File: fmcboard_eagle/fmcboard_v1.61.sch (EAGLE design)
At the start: 208 parts, among them IC1 OPA699ID, IC10 LM358, IC11 7805TV, IC12 SN74AUC2G66DCTR, IC13 SN74AUC2G66DCTR, IC14 SN74AUC2G66DCTR, IC15 SN74AUC2G66DCTR, IC16 DAC7578SPWR, IC17 SN74AUC2G66DCTR, IC18 SN74AUC2G66DCTR, IC19 SN74AUC2G66DCTR, IC2 DAC7578SPWR, IC20 SN74AUC2G66DCTR, IC21 74AUP2GU04GW, IC22 74AUP2GU04GW, IC23 74AUP2GU04GW, IC24 74AUP2GU04GW, IC25 LM358, IC26 AMS1117-1.8, IC3 LTC6229IMS8E#TRPBF, IC4 LTC6229IMS8E#TRPBF, IC5 LTC6229IMS8E#TRPBF, IC6 OPA699ID, IC7 OPA699ID, IC8 LM358, IC9 LM358, J1 8pin, J10 8pin, J11 8pin, J12 4p-2.54, J2 ASP-134604-01, J3 4p-2.54, J4 4p-2.54, J5 8pin, J6 4p-2.54, J7 4p-2.54, J8 4p-2.54, J9 8pin, U1 TXS0108EPWR, U2 STMICROELECTRONICS_L7905ACVST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

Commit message: smd inductors
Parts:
- L1, L2: device rcl:L-US6000-XXX-RC -> SparkFun-Passives:INDUCTOR1210
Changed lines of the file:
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@@
 <part name="SUPPLY30" library="supply2" library_urn="urn:adsk.eagle:library:372" deviceset="GND" device=""/>
 <part name="SUPPLY31" library="supply2" library_urn="urn:adsk.eagle:library:372" deviceset="GND" device=""/>
-<part name="L1" library="rcl" library_urn="urn:adsk.eagle:library:334" deviceset="L-US" device="6000-XXX-RC" package3d_urn="urn:adsk.eagle:package:23538/1" value="10uH"/>
-<part name="L2" library="rcl" library_urn="urn:adsk.eagle:library:334" deviceset="L-US" device="6000-XXX-RC" package3d_urn="urn:adsk.eagle:package:23538/1" value="10uH"/>
+<part name="L1" library="SparkFun-Passives" deviceset="INDUCTOR" device="1210" value="10uH"/>
+<part name="L2" library="SparkFun-Passives" deviceset="INDUCTOR" device="1210" value="10uH"/>
 <part name="C42" library="SparkFun-Passives" deviceset="CAP" device="0805" value="0.1uF"/>
 <part name="C43" library="SparkFun-Passives" deviceset="CAP" device="0805" value="0.1uF"/>

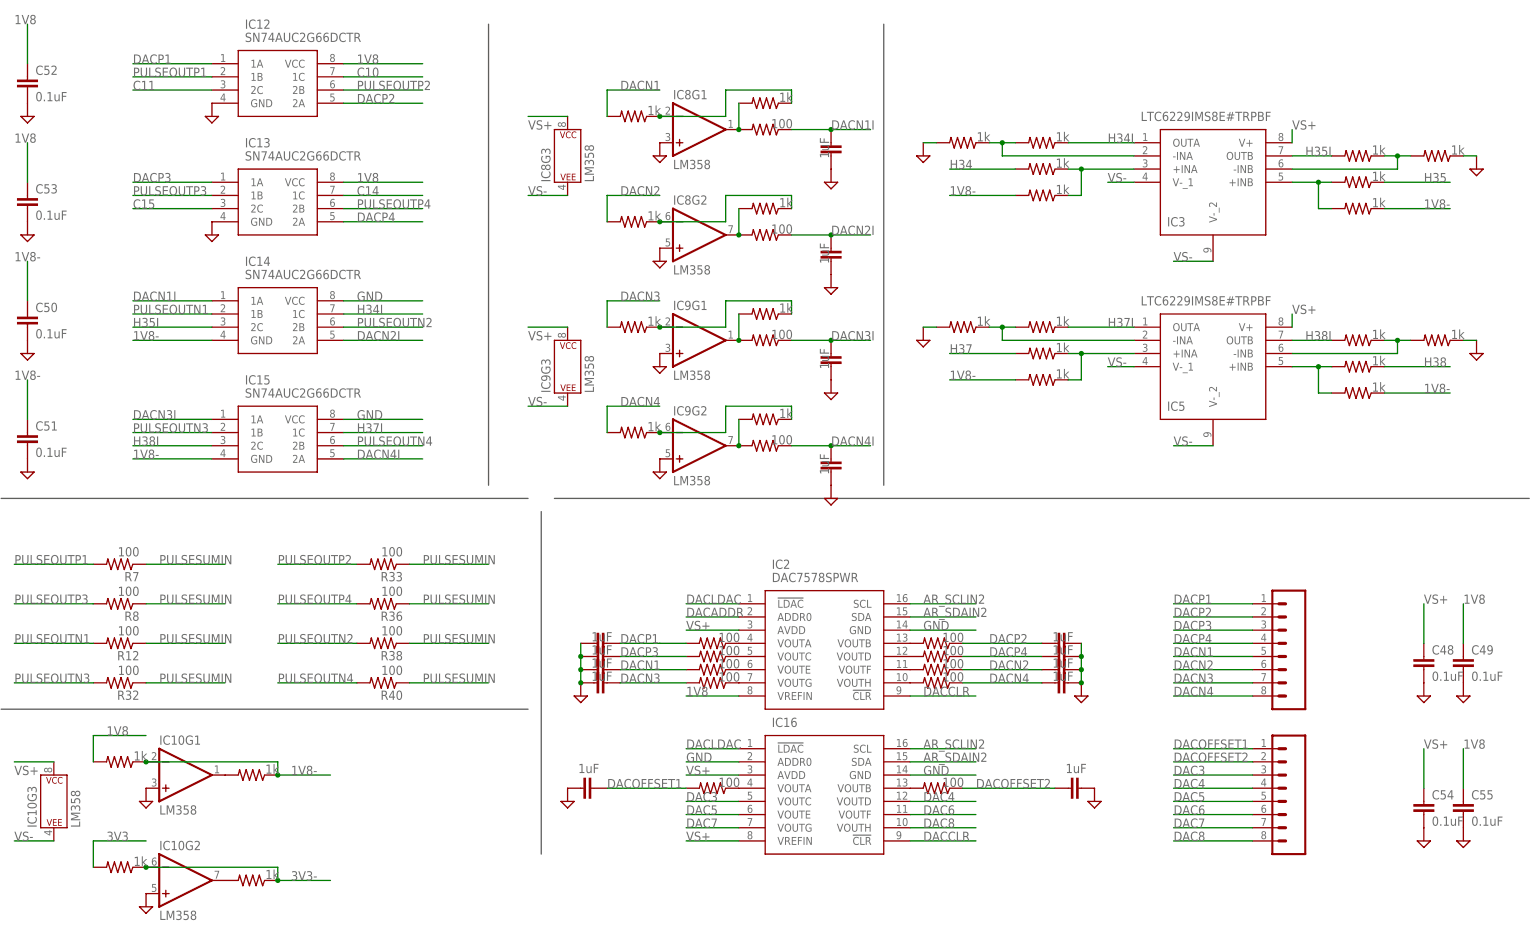
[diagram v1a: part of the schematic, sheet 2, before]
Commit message: v1.61: Fix 1v8- 1k->330 fo 16 100->330 for 9 1pF and 10k pulldown on opin 10k pulldowns on neg pulse inputs
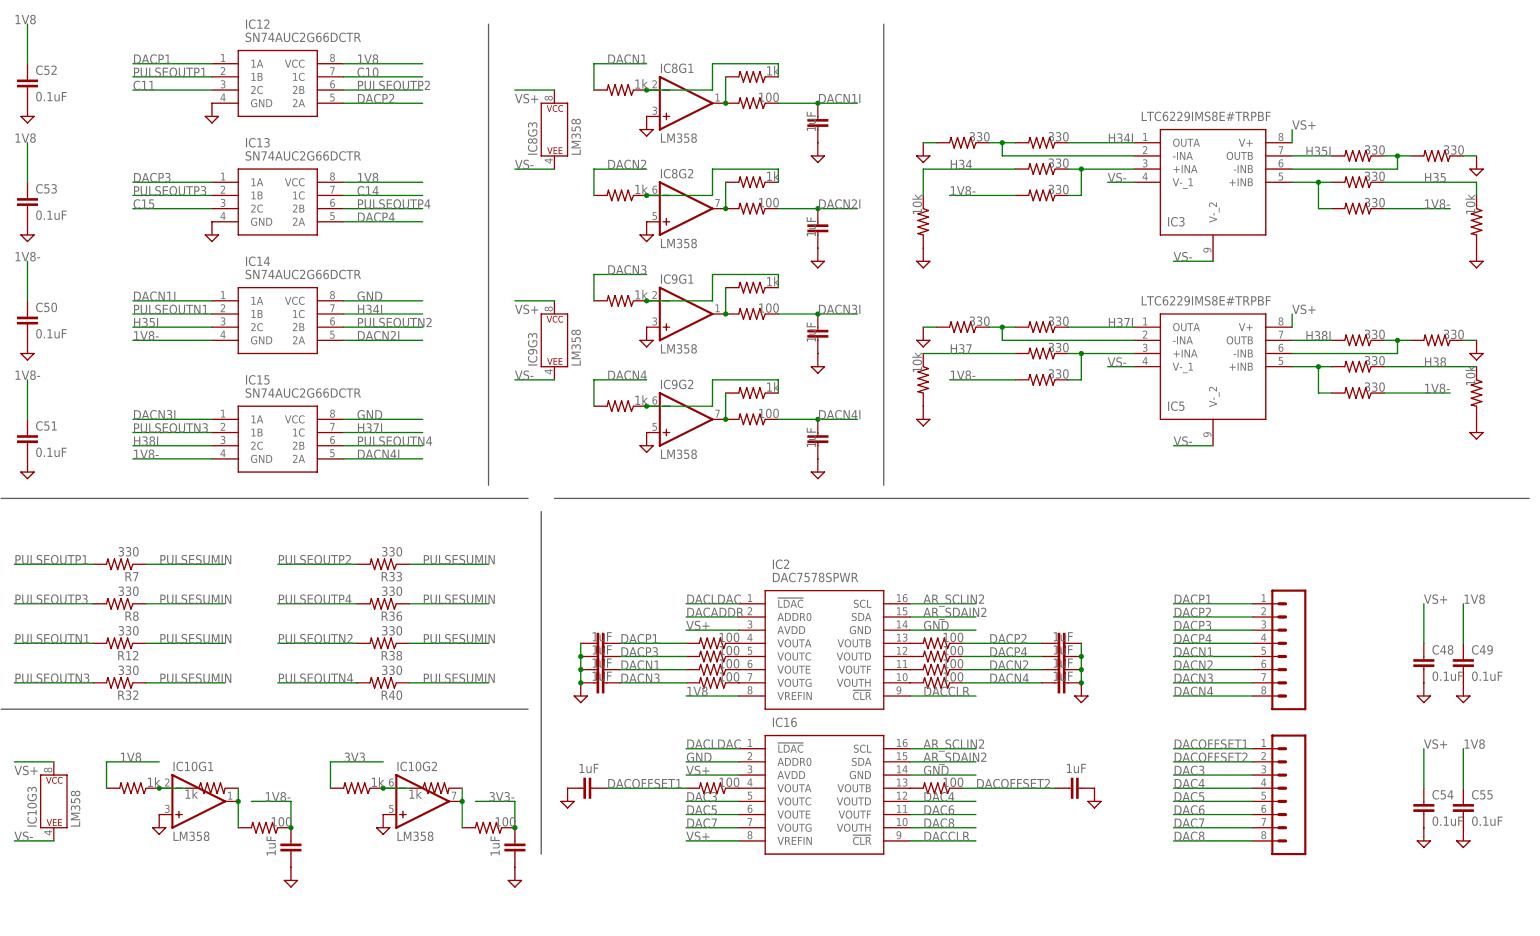
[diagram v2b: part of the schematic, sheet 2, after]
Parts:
- added C77: 1uF, SparkFun-Passives:CAP0805
- added R78, R79: 100, rcl:R-US_R0805
- added R80, R81, R82, R83: 10k, rcl:R-US_R0805
- C32: value 1pF? -> 1uF
- C33: value 1pF? -> 1pF
- R1, R12, R32, R33, R36, R38, R40, R7, R8: value 100 -> 330
- R21, R22, R23, R24, R27, R28, R29, R30, R37, R39, R41, R43, R44, R45, R46, R52: value 1k -> 330
- R42: value 50? -> 1k
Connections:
- new net $N99: IC10G1.-IN, R71.1, R72.1
- new net N$37: IC10G2.-IN, R70.1, R73.1
- net 1V8: no longer J12.P$3
- net 1V8-: now also C77.2, J12.P$3, R78.1; no longer IC10G1.-IN, R71.1, R72.1
- net 3V3: no longer J3.P$4
- net 3V3-: now also C32.2, J3.P$4, R79.1; no longer IC10G2.-IN, R70.1, R73.1
- net GND: now also C32.1, C77.1, R80.2, R81.2, R82.2, R83.2
- net H34: now also R80.1
- net H35: now also R81.1
- net H37: now also R83.1
- net H38: now also R82.1
- net N$35: now also IC10G1.OUT, R71.2, R78.2; no longer IC10G2.OUT, R70.2
- net N$36: now also IC10G2.OUT, R70.2, R79.2; no longer IC10G1.OUT, R71.2
- net PULSESUMIN: no longer C32.1
- net PULSESUMOUT: no longer C32.2
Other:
- moved on the sheet: IC10G1, IC10G2, IC8G1, IC8G2, IC8G3, IC9G1, IC9G2, IC9G3

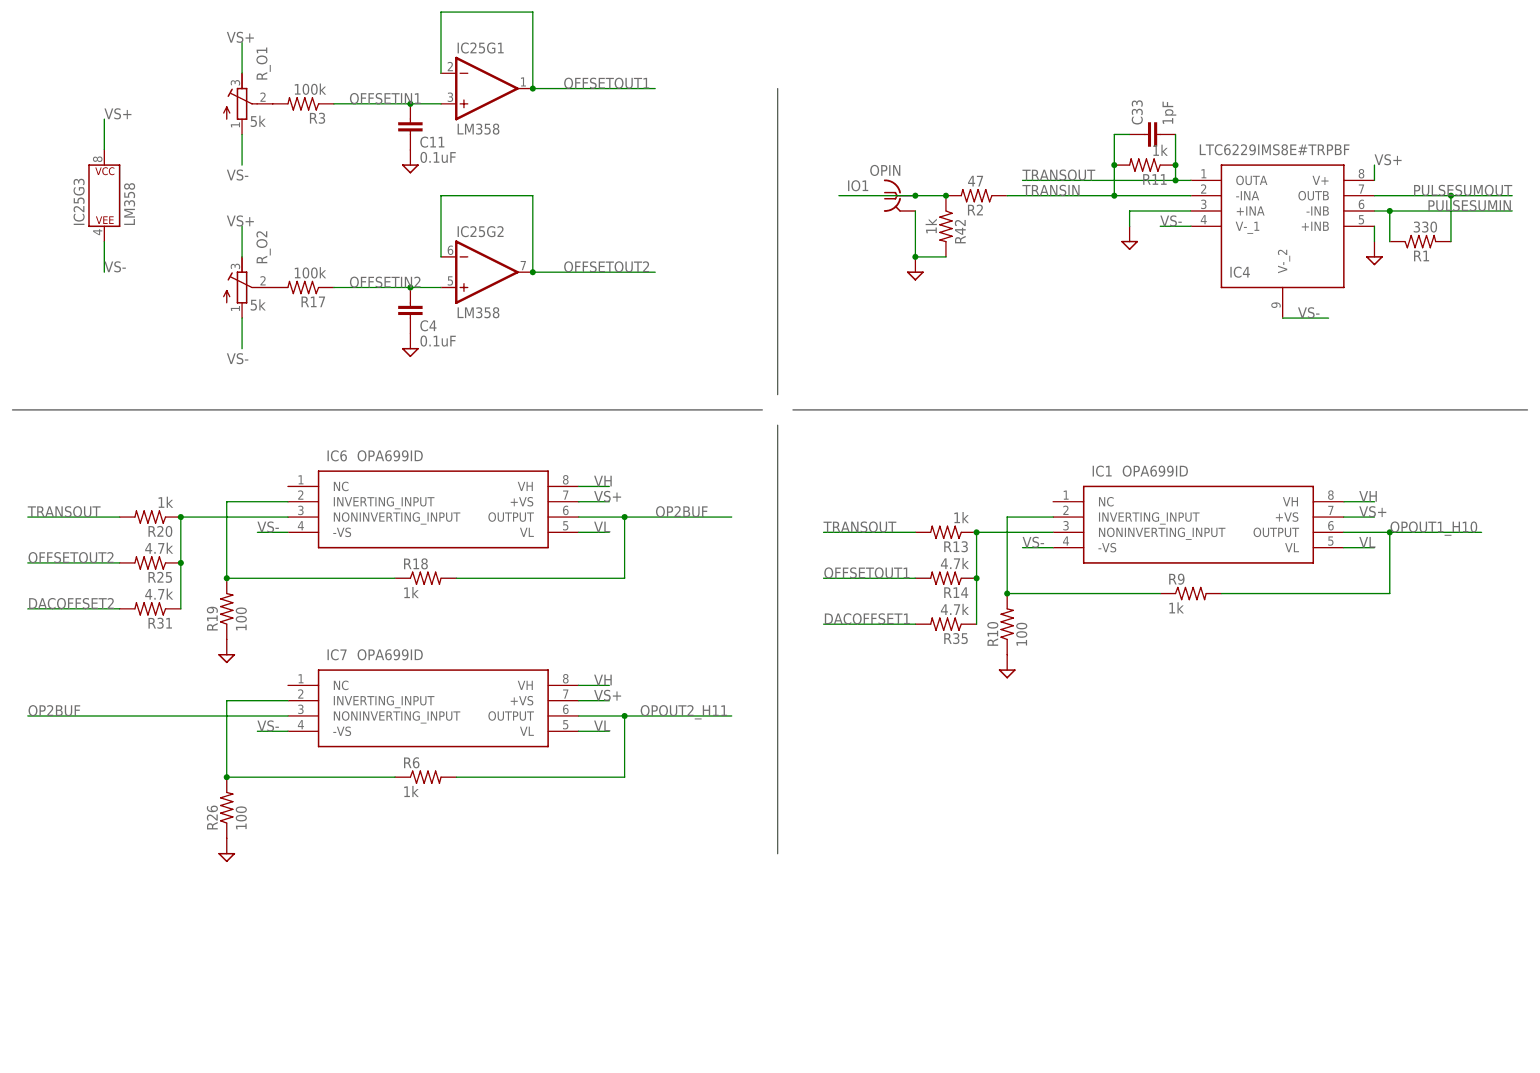
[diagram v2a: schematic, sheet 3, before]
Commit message: v1.61: Add OPA695 for transimpedance and first stage of opin amp
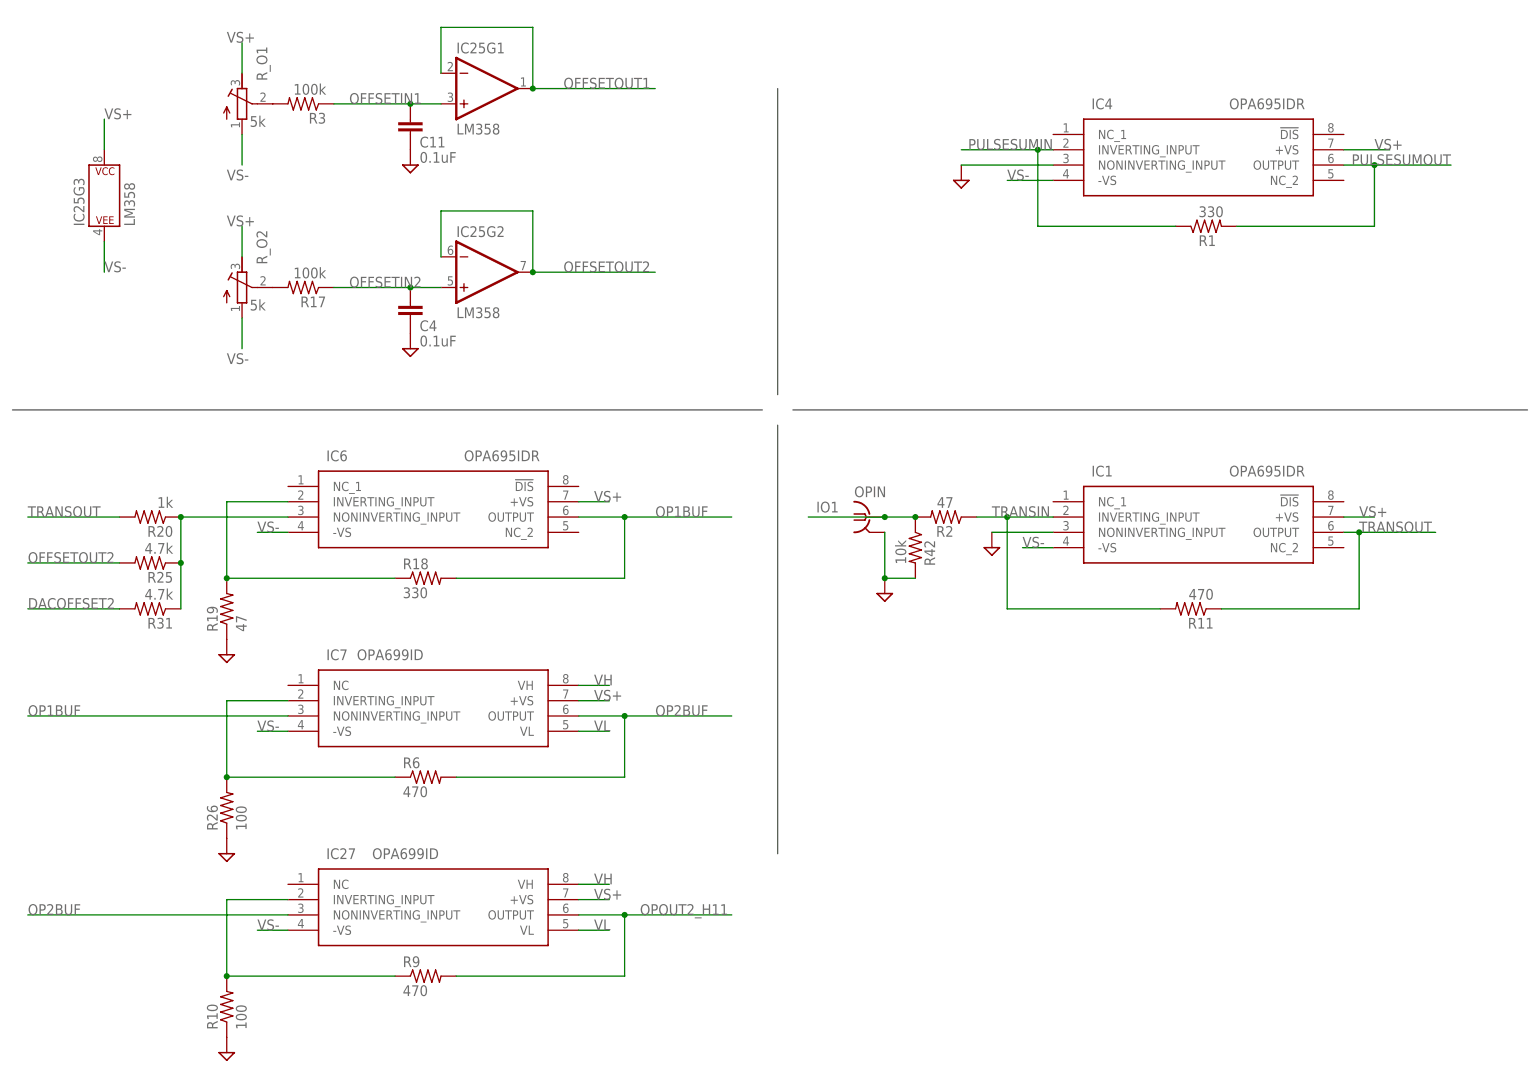
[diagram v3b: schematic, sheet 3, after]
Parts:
- removed C33: 1pF, SparkFun-Passives:CAP0805
- removed R13: 1k, rcl:R-US_R0805
- removed R14, R35: 4.7k, rcl:R-US_R0805
- added C78, C79: 0.1uF, SparkFun-Passives:CAP0805
- added IC27: OPA699ID, OPA699ID:OPA699ID
- IC1, IC6: value OPA699ID -> OPA695IDR; device OPA699ID:OPA699ID -> OPA695IDR:OPA695IDR
- IC4: value LTC6229IMS8E#TRPBF -> OPA695IDR; device LTC6229IMS8E#TRPBF:LTC6229IMS8E#TRPBF -> OPA695IDR:OPA695IDR
- R11, R6, R9: value 1k -> 470
- R18: value 1k -> 330
- R19: value 100 -> 47
- R42: value 1k -> 10k
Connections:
- removed net N$3: IC1.INVERTING_INPUT, R10.2, R9.1
- new net OP1BUF: IC6.OUTPUT, IC7.NONINVERTING_INPUT, J5.3, R18.2
- net DACOFFSET1: no longer R35.2
- net GND: now also C78.2, C79.2, IC1.NONINVERTING_INPUT, IC4.NONINVERTING_INPUT; no longer IC4.+INA, IC4.+INB
- net N$1: now also IC27.INVERTING_INPUT, R10.2, R9.1; no longer IC1.NONINVERTING_INPUT, R13.1, R14.1, R35.1
- net OFFSETOUT1: no longer R14.2
- net OP2BUF: now also IC27.NONINVERTING_INPUT, IC7.OUTPUT, R6.2; no longer IC6.OUTPUT, IC7.NONINVERTING_INPUT, R18.2
- net OPOUT1_H10: no longer IC1.OUTPUT, J5.3, R9.2
- net OPOUT2_H11: now also IC27.OUTPUT, R9.2; no longer IC7.OUTPUT, R6.2
- net PULSESUMIN: now also IC4.INVERTING_INPUT; no longer IC4.-INB
- net PULSESUMOUT: now also IC4.OUTPUT; no longer IC4.OUTB
- net TRANSIN: now also IC1.INVERTING_INPUT; no longer C33.1, IC4.-INA
- net TRANSOUT: now also IC1.OUTPUT; no longer C33.2, IC4.OUTA, R13.2
- net VH: now also IC27.VH; no longer IC1.VH, IC6.VH
- net VL: now also IC27.VL; no longer IC1.VL, IC6.VL
- net VS+: now also C78.1, IC27.+VS, IC4.+VS; no longer IC4.V+
- net VS-: now also C79.1, IC27.-VS, IC4.-VS; no longer IC4.V-_1, IC4.V-_2
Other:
- note removed: "Gain 1 amp"
- moved on the sheet: OPIN, R1, R10, R11, R2, R42, R9

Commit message: routed
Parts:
- removed C11: 0.1uF, SparkFun-Passives:CAP0805
- removed C32, C65: 1uF, SparkFun-Passives:CAP0805
- removed IC25: LM358, SparkFun-IC-Amplifiers:OPAMP-DUALU
- removed J10, J11: 8pin, SparkFun-Connectors:CONN_08"
- removed R3: 100k, rcl:R-US_R0805
- removed R61, R79: 100, rcl:R-US_R0805
- removed R70, R73: 1k, rcl:R-US_R0805
- removed R_O1: 5k, resistor:R-TRIMM3296W
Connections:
- net OPOUT1_H10 renamed H10
- removed net 3V3-: C32.2, J3.P$4, R79.1
- removed net DAC3: IC16.VOUTC, J10.3
- removed net DAC4: IC16.VOUTD, J10.4
- removed net DAC5: IC16.VOUTE, J10.5
- removed net DAC6: IC16.VOUTF, J10.6
- removed net DAC7: IC16.VOUTG, J10.7
- removed net DAC8: IC16.VOUTH, J10.8
- removed net DACOFFSET1: C64.2, J10.1, R60.2
- removed net DACOFFSET2: C65.1, J10.2, R31.2, R61.1
- removed net N$30: IC16.VOUTB, R61.2
- removed net N$36: IC10G2.OUT, R70.2, R79.2
- removed net N$37: IC10G2.-IN, R70.1, R73.1
- removed net N$8: R3.2, R_O1.S
- removed net OFFSETIN1: C11.1, IC25G1.+IN, J5.4, R3.1
- removed net OFFSETIN2: C4.1, IC25G2.+IN, J5.7, R17.1
- removed net OFFSETOUT1: IC25G1.-IN, IC25G1.OUT
- removed net OFFSETOUT2: IC25G2.-IN, IC25G2.OUT, R25.2
- removed net OPOUT2_H11: IC27.OUTPUT, J2.H11, J5.6, R9.2, SV1.5
- new net DACOFFSET: C64.2, J5.6, R31.2, R60.2
- new net OFFSETIN: C4.1, IC10G2.+IN, R17.1
- new net OFFSETOUT: IC10G2.-IN, IC10G2.OUT, J5.5, R25.2
- new net OPOUT_H11: IC27.OUTPUT, J2.H11, J5.8, R9.2, SV1.5
- net 3V3: now also J3.P$4; no longer R73.2
- net GND: now also J5.1, J5.3, J5.7; no longer C11.2, C32.1, C65.2, IC10G2.+IN, J11.1, J11.2, J11.3, J11.4, J11.5, J11.6, J11.7, J11.8
- net IO1: no longer J5.1
- net OP1BUF: no longer J5.3
- net OP2BUF: no longer J5.8
- net TRANSOUT: now also J5.4; no longer J5.5
- net VS+: no longer IC25G3.P$V+, R_O1.E
- net VS-: no longer IC25G3.P$V-, R_O1.A
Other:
- note added: "Make offset and negative 1V8- rails"
- note removed: "Make negative V rails"
- note removed: "Offsets"
- moved on the sheet: C4, R17, R_O2
